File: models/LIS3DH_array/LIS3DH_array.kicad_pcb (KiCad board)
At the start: 2 copper layers, 85 x 89.5 mm, 76 parts, among them J1 Conn_01x08_Socket, J10 Conn_01x09_Socket, J11 Conn_01x03_Socket, J12 Conn_01x02_Socket, J2 Conn_01x08_Socket, J3 Conn_01x08_Socket, J4 Conn_01x08_Socket, J5 Conn_01x08_Socket, J6 Conn_01x08_Socket, J7 Conn_01x08_Socket, J8 Conn_01x08_Socket, J9 Conn_01x08_Socket, U1 LIS3DH, U2 LIS3DH, U3 LIS3DH, U4 LIS3DH, U5 LIS3DH, U6 LIS3DH, U7 LIS3DH, U8 LIS3DH, U9 LIS3DH

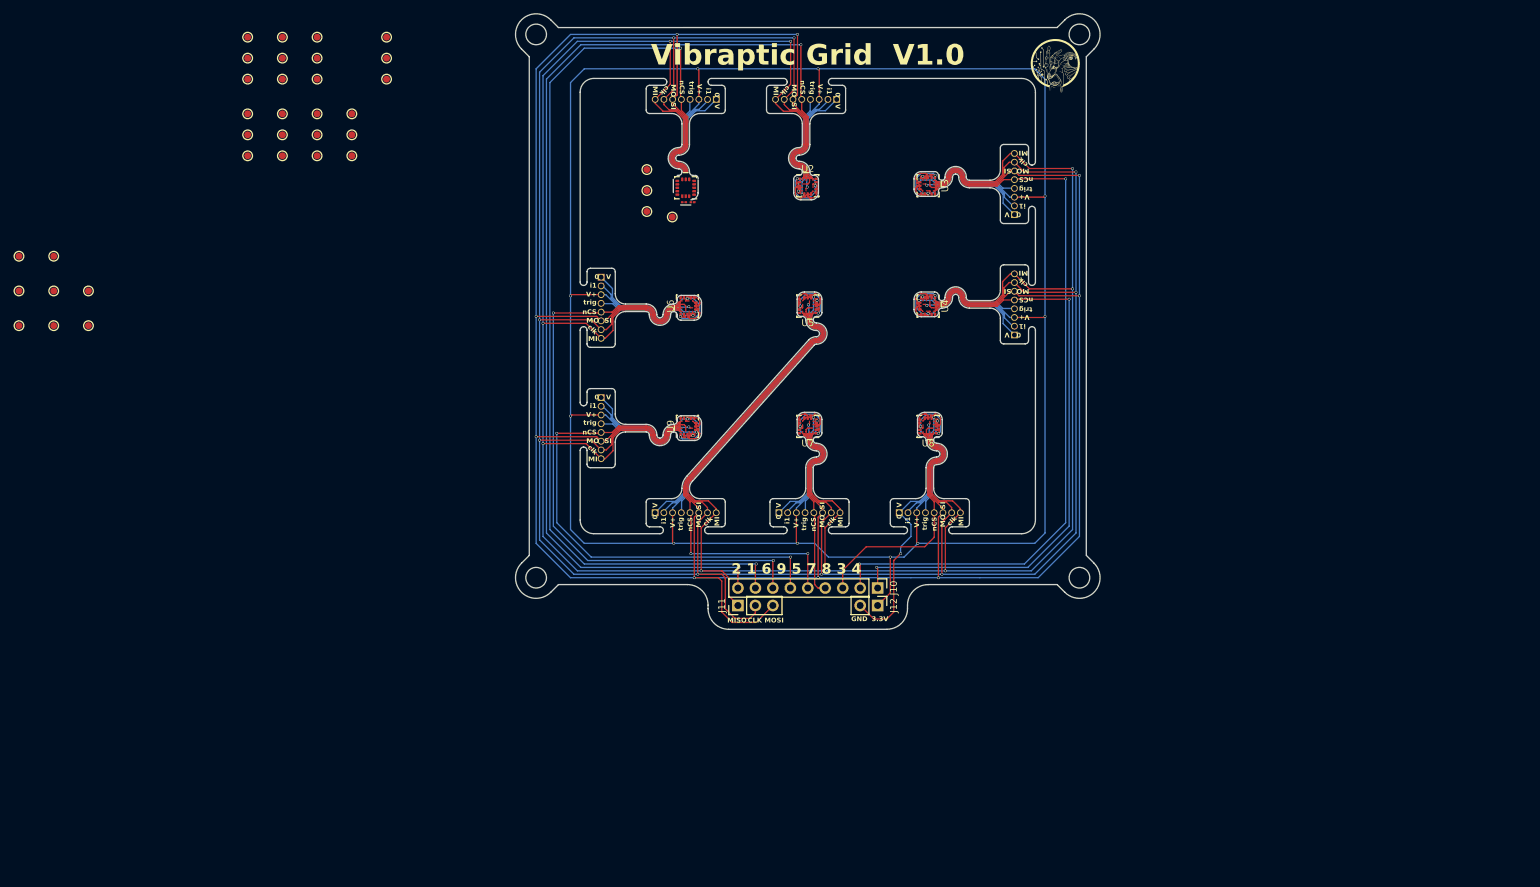
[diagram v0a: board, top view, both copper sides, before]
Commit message: updated LIS3DH array
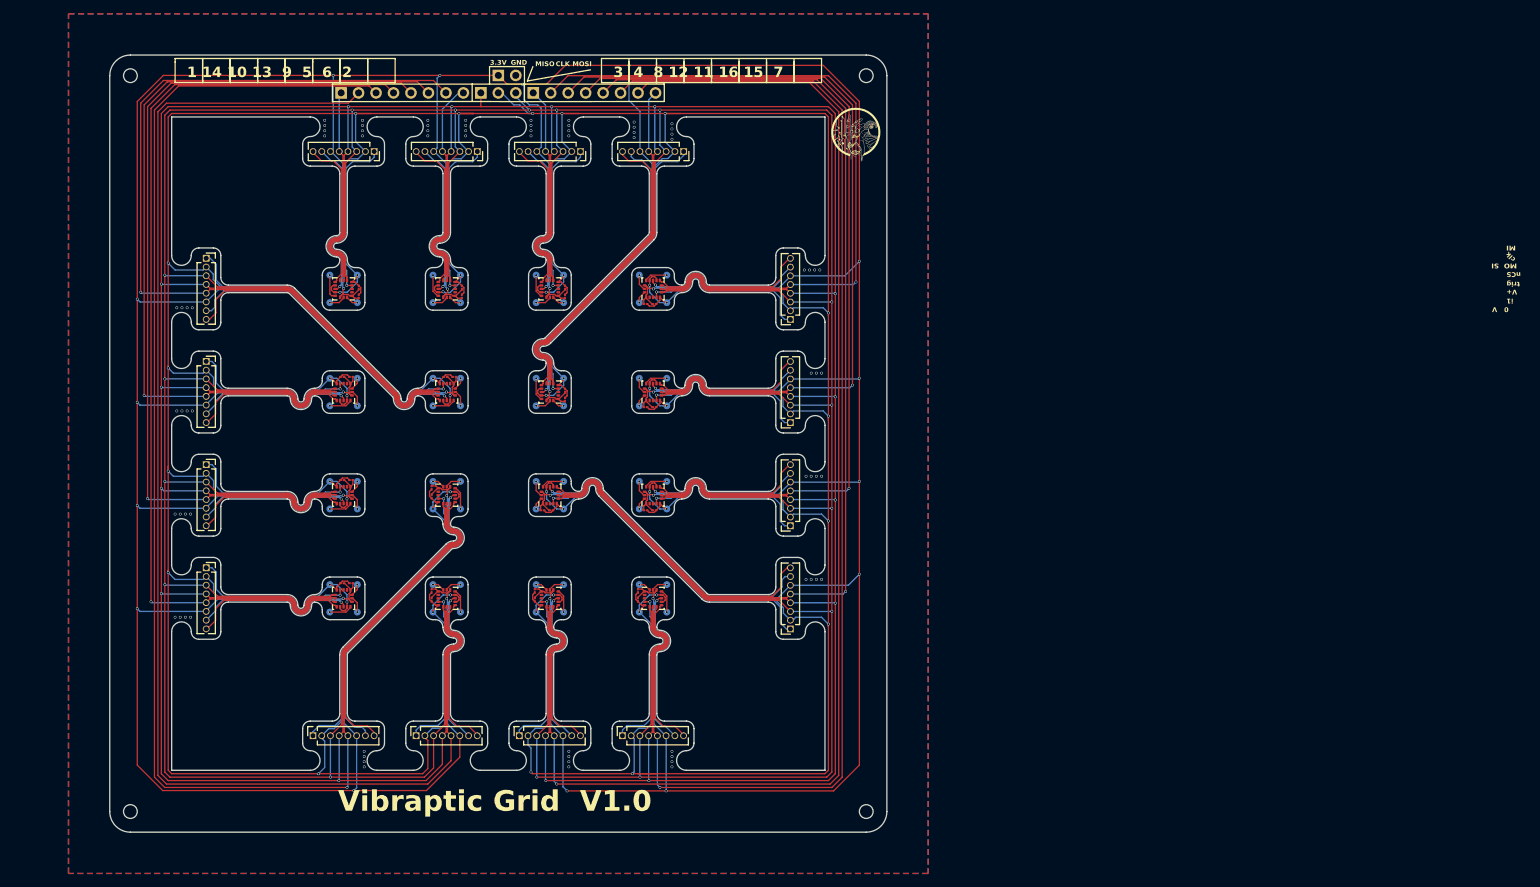
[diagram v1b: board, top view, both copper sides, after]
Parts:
- removed the G*** at (203.5, 47.5)
- added C19: 100n, Capacitor_SMD:C_01005_0402Metric, F.Cu at (112.8, 110.2)
- added C20: 1u, Capacitor_SMD:C_01005_0402Metric, F.Cu at (112.8, 108.9)
- added C21: 100n, Capacitor_SMD:C_01005_0402Metric, F.Cu at (130.2, 112.2)
- added C22: 1u, Capacitor_SMD:C_01005_0402Metric, F.Cu at (128.9, 112.2)
- added C23: 100n, Capacitor_SMD:C_01005_0402Metric, F.Cu at (145.2, 112.2)
- added C24: 1u, Capacitor_SMD:C_01005_0402Metric, F.Cu at (143.9, 112.2)
- added C25: 100n, Capacitor_SMD:C_01005_0402Metric, F.Cu at (99.8, 122.8)
- added C26: 1u, Capacitor_SMD:C_01005_0402Metric, F.Cu at (101.1, 122.8)
- added C27: 100n, Capacitor_SMD:C_01005_0402Metric, F.Cu at (112.8, 125.2)
- added C28: 1u, Capacitor_SMD:C_01005_0402Metric, F.Cu at (112.8, 123.9)
- added C29: 100n, Capacitor_SMD:C_01005_0402Metric, F.Cu at (127.8, 125.2)
- added C30: 1u, Capacitor_SMD:C_01005_0402Metric, F.Cu at (127.8, 123.9)
- added C31: 100n, Capacitor_SMD:C_01005_0402Metric, F.Cu at (142.8, 125.2)
- added C32: 1u, Capacitor_SMD:C_01005_0402Metric, F.Cu at (142.8, 123.9)
- added G***: LOGO, LOGO, F.Cu at (174.5, 57.5)
- added J13: Conn_01x08_Socket, Connector_PinSocket_1.27mm:PinSocket_1x08_P1.27mm_Vertical, F.Cu at (95.5, 145.0)
- added J14: Conn_01x08_Socket, Connector_PinSocket_1.27mm:PinSocket_1x08_P1.27mm_Vertical, F.Cu at (165.0, 129.5)
- added J15: Conn_01x08_Socket, Connector_PinSocket_1.27mm:PinSocket_1x08_P1.27mm_Vertical, F.Cu at (165.0, 114.4)
- added J16: Conn_01x08_Socket, Connector_PinSocket_1.27mm:PinSocket_1x08_P1.27mm_Vertical, F.Cu at (80.0, 120.6)
- added J17: Conn_01x08_Socket, Connector_PinSocket_1.27mm:PinSocket_1x08_P1.27mm_Vertical, F.Cu at (110.6, 145.0)
- added J18: Conn_01x08_Socket, Connector_PinSocket_1.27mm:PinSocket_1x08_P1.27mm_Vertical, F.Cu at (125.6, 145.0)
- added J19: Conn_01x08_Socket, Connector_PinSocket_1.27mm:PinSocket_1x08_P1.27mm_Vertical, F.Cu at (140.6, 145.0)
- added J20: Conn_01x09_Socket, Connector_PinHeader_2.54mm:PinHeader_1x08_P2.54mm_Vertical, F.Cu at (99.6, 51.5)
- added TP37: TestPoint, TestPoint:TestPoint_Pad_D1.0mm, B.Cu at (113.0, 108.0)
- added TP38: TestPoint, TestPoint:TestPoint_Pad_D1.0mm, B.Cu at (117.0, 108.0)
- added TP39: TestPoint, TestPoint:TestPoint_Pad_D1.0mm, B.Cu at (117.0, 112.0)
- added TP40: TestPoint, TestPoint:TestPoint_Pad_D1.0mm, B.Cu at (113.0, 112.0)
- added TP41: TestPoint, TestPoint:TestPoint_Pad_D1.0mm, B.Cu at (128.0, 112.0)
- added TP42: TestPoint, TestPoint:TestPoint_Pad_D1.0mm, B.Cu at (128.0, 108.0)
- added TP43: TestPoint, TestPoint:TestPoint_Pad_D1.0mm, B.Cu at (132.0, 108.0)
- added TP44: TestPoint, TestPoint:TestPoint_Pad_D1.0mm, B.Cu at (132.0, 112.0)
- added TP45: TestPoint, TestPoint:TestPoint_Pad_D1.0mm, B.Cu at (143.0, 112.0)
- added TP46: TestPoint, TestPoint:TestPoint_Pad_D1.0mm, B.Cu at (143.0, 108.0)
- added TP47: TestPoint, TestPoint:TestPoint_Pad_D1.0mm, B.Cu at (147.0, 108.0)
- added TP48: TestPoint, TestPoint:TestPoint_Pad_D1.0mm, B.Cu at (147.0, 112.0)
- added TP49: TestPoint, TestPoint:TestPoint_Pad_D1.0mm, B.Cu at (102.0, 123.0)
- added TP50: TestPoint, TestPoint:TestPoint_Pad_D1.0mm, B.Cu at (102.0, 127.0)
- added TP51: TestPoint, TestPoint:TestPoint_Pad_D1.0mm, B.Cu at (98.0, 127.0)
- added TP52: TestPoint, TestPoint:TestPoint_Pad_D1.0mm, B.Cu at (98.0, 123.0)
- added TP53: TestPoint, TestPoint:TestPoint_Pad_D1.0mm, B.Cu at (113.0, 123.0)
- added TP54: TestPoint, TestPoint:TestPoint_Pad_D1.0mm, B.Cu at (117.0, 123.0)
- added TP55: TestPoint, TestPoint:TestPoint_Pad_D1.0mm, B.Cu at (117.0, 127.0)
- added TP56: TestPoint, TestPoint:TestPoint_Pad_D1.0mm, B.Cu at (113.0, 127.0)
- added TP57: TestPoint, TestPoint:TestPoint_Pad_D1.0mm, B.Cu at (128.0, 123.0)
- added TP58: TestPoint, TestPoint:TestPoint_Pad_D1.0mm, B.Cu at (132.0, 123.0)
- added TP59: TestPoint, TestPoint:TestPoint_Pad_D1.0mm, B.Cu at (132.0, 127.0)
- added TP60: TestPoint, TestPoint:TestPoint_Pad_D1.0mm, B.Cu at (128.0, 127.0)
- added TP61: TestPoint, TestPoint:TestPoint_Pad_D1.0mm, B.Cu at (143.0, 123.0)
- added TP62: TestPoint, TestPoint:TestPoint_Pad_D1.0mm, B.Cu at (147.0, 123.0)
- added TP63: TestPoint, TestPoint:TestPoint_Pad_D1.0mm, B.Cu at (147.0, 127.0)
- added TP64: TestPoint, TestPoint:TestPoint_Pad_D1.0mm, B.Cu at (143.0, 127.0)
- added U10: LIS3DH, Package_LGA:LGA-16_3x3mm_P0.5mm_LayoutBorder3x5y, F.Cu at (115.0, 110.0)
- added U11: LIS3DH, Package_LGA:LGA-16_3x3mm_P0.5mm_LayoutBorder3x5y, F.Cu at (130.0, 110.0)
- added U12: LIS3DH, Package_LGA:LGA-16_3x3mm_P0.5mm_LayoutBorder3x5y, F.Cu at (145.0, 110.0)
- added U13: LIS3DH, Package_LGA:LGA-16_3x3mm_P0.5mm_LayoutBorder3x5y, F.Cu at (100.0, 125.0)
- added U14: LIS3DH, Package_LGA:LGA-16_3x3mm_P0.5mm_LayoutBorder3x5y, F.Cu at (115.0, 125.0)
- added U15: LIS3DH, Package_LGA:LGA-16_3x3mm_P0.5mm_LayoutBorder3x5y, F.Cu at (130.0, 125.0)
- added U16: LIS3DH, Package_LGA:LGA-16_3x3mm_P0.5mm_LayoutBorder3x5y, F.Cu at (145.0, 125.0)
- J10: footprint Connector_PinHeader_2.54mm:PinHeader_1x09_P2.54mm_Vertical -> Connector_PinHeader_2.54mm:PinHeader_1x08_P2.54mm_Vertical
- TP1, TP10, TP11, TP12, TP13, TP14, TP15, TP16, TP17, TP18, TP19, TP2, TP20, TP21, TP22, TP23, TP24, TP25, TP26, TP27, TP28, TP29, TP3, TP30, TP31, TP32, TP33, TP34, TP35, TP36, TP4, TP5, TP6, TP7, TP8, TP9: moved to B.Cu
- moved J12 94.8 mm to (122.5, 49.0), turned to 90 degrees
- moved TP35 89.9 mm to (147.0, 97.0), turned to 180 degrees
- moved TP31 89.4 mm to (147.0, 82.0), turned to 180 degrees
- moved J10 87.7 mm to (127.6, 51.5), turned to 90 degrees
- moved J11 83.4 mm to (120.0, 51.5)
- moved TP34 69.5 mm to (132.0, 93.0), turned to -90 degrees
- moved TP30 69.1 mm to (132.0, 78.0), turned to -90 degrees
- moved C9 68.9 mm to (99.8, 92.8)
- moved J5 68.9 mm to (80.0, 90.6), turned to 0 degrees
- moved C10 68.8 mm to (101.1, 92.8), turned to 180 degrees
- moved U5 68.6 mm to (100.0, 95.0), turned to -90 degrees
- moved TP18 67.5 mm to (102.0, 112.0)
- moved TP9 66.5 mm to (102.0, 108.0)
- moved TP29 64.2 mm to (117.0, 78.0), turned to -90 degrees
- moved J3 63.8 mm to (134.4, 60.0), turned to -90 degrees
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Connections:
- J1 pad 1: VDD -> GND
- J1 pad 2: GND -> Sclk
- J1 pad 3: nCS_1 -> SDI
- J1 pad 4: SDI -> SDO
- J1 pad 5: Sclk -> nCS_1
- J1 pad 6: SDO -> VDD
- J10 pad 1: nCS_4 -> nCS_3
- J10 pad 2: nCS_3 -> nCS_4
- J10 pad 4: nCS_7 -> nCS_12
- J10 pad 5: nCS_5 -> nCS_11
- J10 pad 6: nCS_9 -> nCS_16
- J10 pad 7: nCS_6 -> nCS_15
- J10 pad 8: nCS_1 -> nCS_7
- J2 pad 1: VDD -> GND
- J2 pad 2: GND -> Sclk
- J2 pad 3: nCS_2 -> SDI
- J2 pad 4: SDI -> SDO
- J2 pad 5: Sclk -> nCS_2
- J2 pad 6: SDO -> VDD
- J3 pad 1: VDD -> GND
- J3 pad 2: GND -> Sclk
- J3 pad 3: nCS_3 -> SDI
- J3 pad 4: SDI -> SDO
- J3 pad 5: Sclk -> nCS_3
- J3 pad 6: SDO -> VDD
- J4 pad 1: VDD -> GND
- J4 pad 2: GND -> Sclk
- J4 pad 3: nCS_4 -> SDI
- J4 pad 4: SDI -> SDO
- J4 pad 5: Sclk -> nCS_4
- J4 pad 6: SDO -> VDD
- J5 pad 1: VDD -> GND
- J5 pad 2: GND -> Sclk
- J5 pad 3: nCS_5 -> SDI
- J5 pad 4: SDI -> SDO
- J5 pad 5: Sclk -> nCS_5
- J5 pad 6: SDO -> VDD
- J6 pad 1: VDD -> GND
- J6 pad 2: GND -> Sclk
- J6 pad 3: nCS_6 -> SDI
- J6 pad 4: SDI -> SDO
- J6 pad 5: Sclk -> nCS_6
- J6 pad 6: SDO -> VDD
- J7 pad 1: VDD -> GND
- J7 pad 2: GND -> Sclk
- J7 pad 3: nCS_7 -> SDI
- J7 pad 4: SDI -> SDO
- J7 pad 5: Sclk -> nCS_7
- J7 pad 6: SDO -> VDD
- J8 pad 1: VDD -> GND
- J8 pad 2: GND -> Sclk
- J8 pad 3: nCS_8 -> SDI
- J8 pad 4: SDI -> SDO
- J8 pad 5: Sclk -> nCS_8
- J8 pad 6: SDO -> VDD
- J9 pad 1: VDD -> GND
- J9 pad 2: GND -> Sclk
- J9 pad 3: nCS_9 -> SDI
- J9 pad 4: SDI -> SDO
- J9 pad 5: Sclk -> nCS_9
- J9 pad 6: SDO -> VDD
- U1 pad 10: unconnected-(U1-GND-Pad10) -> GND
- U1 pad 12: unconnected-(U1-GND-Pad12) -> GND
- U2 pad 10: unconnected-(U2-GND-Pad10) -> GND
- U2 pad 12: unconnected-(U2-GND-Pad12) -> GND
- U3 pad 10: unconnected-(U3-GND-Pad10) -> GND
- U3 pad 12: unconnected-(U3-GND-Pad12) -> GND
- U4 pad 10: unconnected-(U4-GND-Pad10) -> GND
- U4 pad 12: unconnected-(U4-GND-Pad12) -> GND
- U5 pad 10: unconnected-(U5-GND-Pad10) -> GND
- U5 pad 12: unconnected-(U5-GND-Pad12) -> GND
- U6 pad 10: unconnected-(U6-GND-Pad10) -> GND
- U6 pad 12: unconnected-(U6-GND-Pad12) -> GND
- U7 pad 10: unconnected-(U7-GND-Pad10) -> GND
- U7 pad 12: unconnected-(U7-GND-Pad12) -> GND
- U8 pad 10: unconnected-(U8-GND-Pad10) -> GND
- U8 pad 12: unconnected-(U8-GND-Pad12) -> GND
- U9 pad 10: unconnected-(U9-GND-Pad10) -> GND
- U9 pad 12: unconnected-(U9-GND-Pad12) -> GND
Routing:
- net VDD: track 553.6 -> 1102.6 mm, vias 18 -> 31
- net Sclk: track 506.7 -> 963.6 mm, vias 17 -> 32
- net SDO: track 503.8 -> 903.7 mm, vias 9 -> 15
- net SDI: track 529.4 -> 904.2 mm, vias 9 -> 16
- net nCS_10: track 0.00 -> 210.2 mm, vias 0 -> 1
- net nCS_15: track 0.00 -> 197.8 mm, vias 0 -> 1
- net nCS_14: track 0.00 -> 196.0 mm
- net GND: track 448.4 -> 640.8 mm, vias 25 -> 107
- net nCS_16: track 0.00 -> 187.5 mm, vias 0 -> 1
- net nCS_11: track 0.00 -> 159.1 mm, vias 0 -> 1
- net (no net): track 156.4 -> 0.00 mm
- net nCS_13: track 0.00 -> 138.0 mm, vias 0 -> 1
- net nCS_2: track 160.6 -> 31.2 mm, vias 2 -> 0
- net nCS_12: track 0.00 -> 126.0 mm, vias 0 -> 1
- net nCS_1: track 142.1 -> 29.6 mm, vias 2 -> 0
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- added copper zone on B.Cu, net GND
- added copper zone on F.Cu, net GND
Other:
- board size 85 x 89.5 mm -> 113 x 113 mm
- board text added: "1 14 10 13 9 5 6 2"
- board text added: "3 4 8 12 11 16 15 7"
- board text added: "Acc1"
- board text added: "Acc10"
- board text added: "Acc11"
- board text added: "Acc12"
- board text added: "Acc13"
- board text added: "Acc14"
- board text added: "Acc15"
- board text added: "Acc16"
- board text added: "Acc2"
- board text added: "Acc3"
- board text added: "Acc4"
- board text added: "Acc5"
- board text added: "Acc6"
- board text added: "Acc7"
- board text added: "Acc8"
- board text added: "Acc9"
- board text removed: "2 1 6 9 5 7 8 3 4"

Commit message: updated lis3dh array: fpc connectors
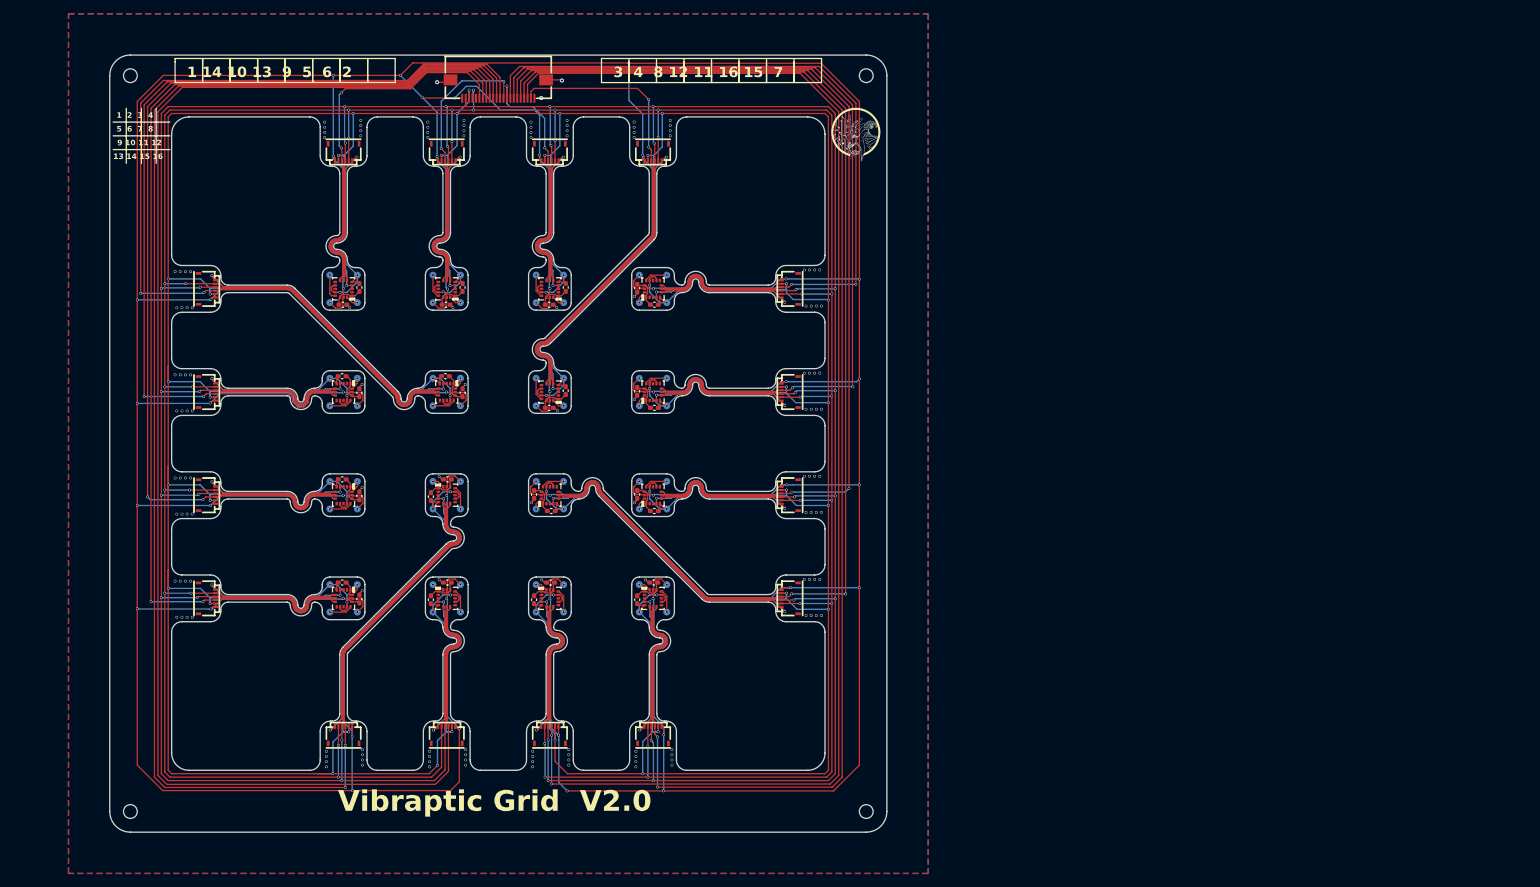
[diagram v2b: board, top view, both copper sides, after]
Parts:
- removed J1, J13, J14, J15, J16, J17, J18, J19, J2, J3, J4, J5, J6, J7, J8, J9: Conn_01x08_Socket, Connector_PinSocket_1.27mm:PinSocket_1x08_P1.27mm_Vertical
- removed J10, J20: Conn_01x09_Socket, Connector_PinHeader_2.54mm:PinHeader_1x08_P2.54mm_Vertical
- removed J11: Conn_01x03_Socket, Connector_PinHeader_2.54mm:PinHeader_1x03_P2.54mm_Vertical
- removed J12: Conn_01x02_Socket, Connector_PinHeader_2.54mm:PinHeader_1x02_P2.54mm_Vertical
- added FPC1: HC-FPC-05-09-6RLTAG, 00_lcsc:FPC-SMD_6P-P0.50_HC-FPC-05-09-6RLTAG, F.Cu at (100.0, 60.2)
- added FPC10: HC-FPC-05-09-6RLTAG, 00_lcsc:FPC-SMD_6P-P0.50_HC-FPC-05-09-6RLTAG, F.Cu at (100.0, 144.8)
- added FPC11: HC-FPC-05-09-6RLTAG, 00_lcsc:FPC-SMD_6P-P0.50_HC-FPC-05-09-6RLTAG, F.Cu at (164.8, 125.0)
- added FPC12: HC-FPC-05-09-6RLTAG, 00_lcsc:FPC-SMD_6P-P0.50_HC-FPC-05-09-6RLTAG, F.Cu at (164.8, 110.0)
- added FPC13: HC-FPC-05-09-6RLTAG, 00_lcsc:FPC-SMD_6P-P0.50_HC-FPC-05-09-6RLTAG, F.Cu at (80.2, 125.0)
- added FPC14: HC-FPC-05-09-6RLTAG, 00_lcsc:FPC-SMD_6P-P0.50_HC-FPC-05-09-6RLTAG, F.Cu at (115.0, 144.8)
- added FPC15: HC-FPC-05-09-6RLTAG, 00_lcsc:FPC-SMD_6P-P0.50_HC-FPC-05-09-6RLTAG, F.Cu at (130.0, 144.8)
- added FPC16: HC-FPC-05-09-6RLTAG, 00_lcsc:FPC-SMD_6P-P0.50_HC-FPC-05-09-6RLTAG, F.Cu at (145.0, 144.8)
- added FPC17: AFC01-S22FCA-00, 00_lcsc:FPC-SMD_P0.5-22P_FGS-XJ-H2.0, F.Cu at (122.5, 50.9)
- added FPC2: HC-FPC-05-09-6RLTAG, 00_lcsc:FPC-SMD_6P-P0.50_HC-FPC-05-09-6RLTAG, F.Cu at (115.0, 60.2)
- added FPC3: HC-FPC-05-09-6RLTAG, 00_lcsc:FPC-SMD_6P-P0.50_HC-FPC-05-09-6RLTAG, F.Cu at (130.0, 60.2)
- added FPC4: HC-FPC-05-09-6RLTAG, 00_lcsc:FPC-SMD_6P-P0.50_HC-FPC-05-09-6RLTAG, F.Cu at (164.8, 80.0)
- added FPC5: HC-FPC-05-09-6RLTAG, 00_lcsc:FPC-SMD_6P-P0.50_HC-FPC-05-09-6RLTAG, F.Cu at (80.2, 95.0)
- added FPC6: HC-FPC-05-09-6RLTAG, 00_lcsc:FPC-SMD_6P-P0.50_HC-FPC-05-09-6RLTAG, F.Cu at (80.2, 80.0)
- added FPC7: HC-FPC-05-09-6RLTAG, 00_lcsc:FPC-SMD_6P-P0.50_HC-FPC-05-09-6RLTAG, F.Cu at (145.0, 60.2)
- added FPC8: HC-FPC-05-09-6RLTAG, 00_lcsc:FPC-SMD_6P-P0.50_HC-FPC-05-09-6RLTAG, F.Cu at (164.8, 95.0)
- added FPC9: HC-FPC-05-09-6RLTAG, 00_lcsc:FPC-SMD_6P-P0.50_HC-FPC-05-09-6RLTAG, F.Cu at (80.2, 110.0)
- C1, C10, C11, C12, C13, C14, C15, C16, C17, C18, C19, C2, C20, C21, C22, C23, C24, C25, C26, C27, C28, C29, C3, C30, C31, C32, C4, C5, C6, C7, C8, C9: footprint Capacitor_SMD:C_01005_0402Metric -> Capacitor_SMD:C_0402_1005Metric_Pad0.74x0.62mm_HandSolder
- U1, U10, U11, U12, U13, U14, U15, U16, U2, U3, U4, U5, U6, U7, U8, U9: footprint Package_LGA:LGA-16_3x3mm_P0.5mm_LayoutBorder3x5y -> 00_custom-footprints:LGA-16_3x3mm_P0.5mm_LayoutBorder3x5y
- moved C2 2.59 mm to (99.9, 82.3), turned to 0 degrees
- moved C4 2.59 mm to (114.9, 82.3), turned to 0 degrees
- moved C14 2.59 mm to (129.9, 97.3), turned to 0 degrees
- moved C6 2.59 mm to (129.9, 82.3), turned to 0 degrees
- moved C16 2.59 mm to (142.7, 94.9), turned to -90 degrees
- moved C24 2.59 mm to (142.7, 109.9), turned to -90 degrees
- moved C8 2.59 mm to (142.7, 79.9), turned to -90 degrees
- moved C10 2.59 mm to (102.3, 95.1), turned to 90 degrees
- moved C12 2.59 mm to (117.3, 95.1), turned to 90 degrees
- moved C18 2.59 mm to (102.3, 110.1), turned to 90 degrees
- moved C20 2.59 mm to (115.1, 107.7), turned to 180 degrees
- moved C22 2.59 mm to (127.7, 109.9), turned to -90 degrees
- moved C26 2.59 mm to (102.3, 125.1), turned to 90 degrees
- moved C28 2.59 mm to (115.1, 122.7), turned to 180 degrees
- moved C30 2.59 mm to (130.1, 122.7), turned to 180 degrees
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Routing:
- net /LIS3DH_unit6/INT1: track 49.9 -> 0.00 mm, vias 1 -> 0
- net /LIS3DH_unit11/INT1: track 49.9 -> 0.00 mm, vias 1 -> 0
- net /LIS3DH_unit10/INT1: track 49.9 -> 0.00 mm, vias 1 -> 0
- net /LIS3DH_unit7/INT1: track 49.9 -> 0.00 mm, vias 1 -> 0
- net /LIS3DH_unit11/INT2: track 45.8 -> 0.00 mm
- net /LIS3DH_unit10/INT2: track 45.8 -> 0.00 mm
- net /LIS3DH_unit6/INT2: track 45.8 -> 0.00 mm
- net /LIS3DH_unit7/INT2: track 45.8 -> 0.00 mm
- net GND: track 640.8 -> 595.6 mm, vias 107 -> 195
- net /LIS3DH_unit2/INT1: track 33.6 -> 0.00 mm, vias 1 -> 0
- net /LIS3DH_unit1/INT1: track 33.6 -> 0.00 mm, vias 1 -> 0
- net /LIS3DH_unit9/INT1: track 33.6 -> 0.00 mm, vias 1 -> 0
- net /LIS3DH_unit5/INT1: track 33.6 -> 0.00 mm, vias 1 -> 0
- net /LIS3DH_unit16/INT1: track 33.6 -> 0.00 mm, vias 1 -> 0
- net /LIS3DH_unit15/INT1: track 33.6 -> 0.00 mm, vias 1 -> 0
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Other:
- outline, holes or cut-outs redrawn
- board text added: "1 2 3 4"
- board text added: "13 14 15 16"
- board text added: "5 6 7 8"
- board text added: "9 10 11 12"
- board text added: "Vibraptic Grid V2.0"
- board text removed: "0 V"
- board text removed: "3.3V"
- board text removed: "CLK"
- board text removed: "GND"
- board text removed: "MI"
- board text removed: "MISO"
- board text removed: "MO SI"
- board text removed: "MOSI"
- board text removed: "V+"
- board text removed: "Vibraptic Grid V1.0"
- board text removed: "clk"
- board text removed: "i1"
- board text removed: "nCS"
- board text removed: "trig"

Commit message: updated
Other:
- board text added: "Vibraptic Grid V2.1"
- board text removed: "Vibraptic Grid V2.0"
